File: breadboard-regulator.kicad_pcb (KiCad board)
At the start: 2 copper layers, 138.7 x 25.9 mm, 18 parts, among them J1 Barrel_Jack_Switch, J2 Conn_01x02_Pin, J3 Conn_01x02_Pin, U1 LM7805_TO220, U3 LD1117V33_TO-220

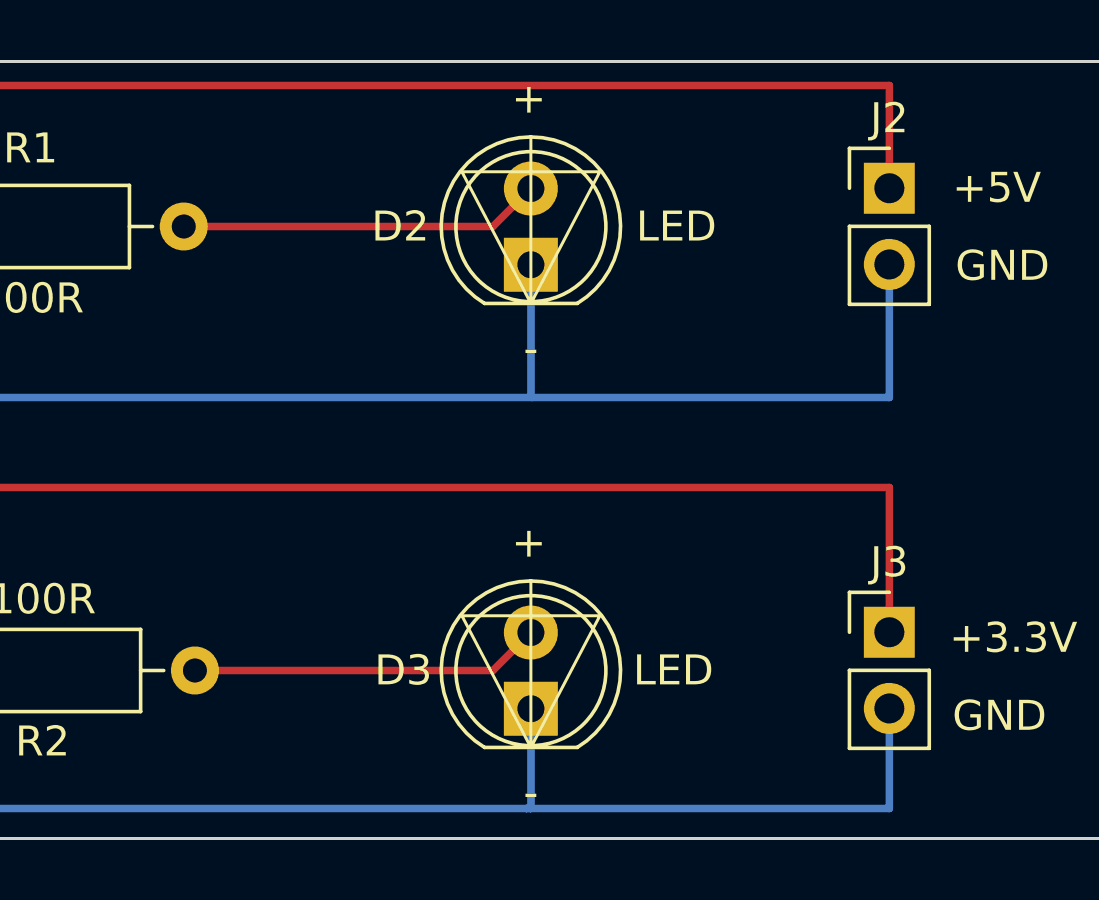
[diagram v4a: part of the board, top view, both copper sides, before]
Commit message: add new beginner pin header
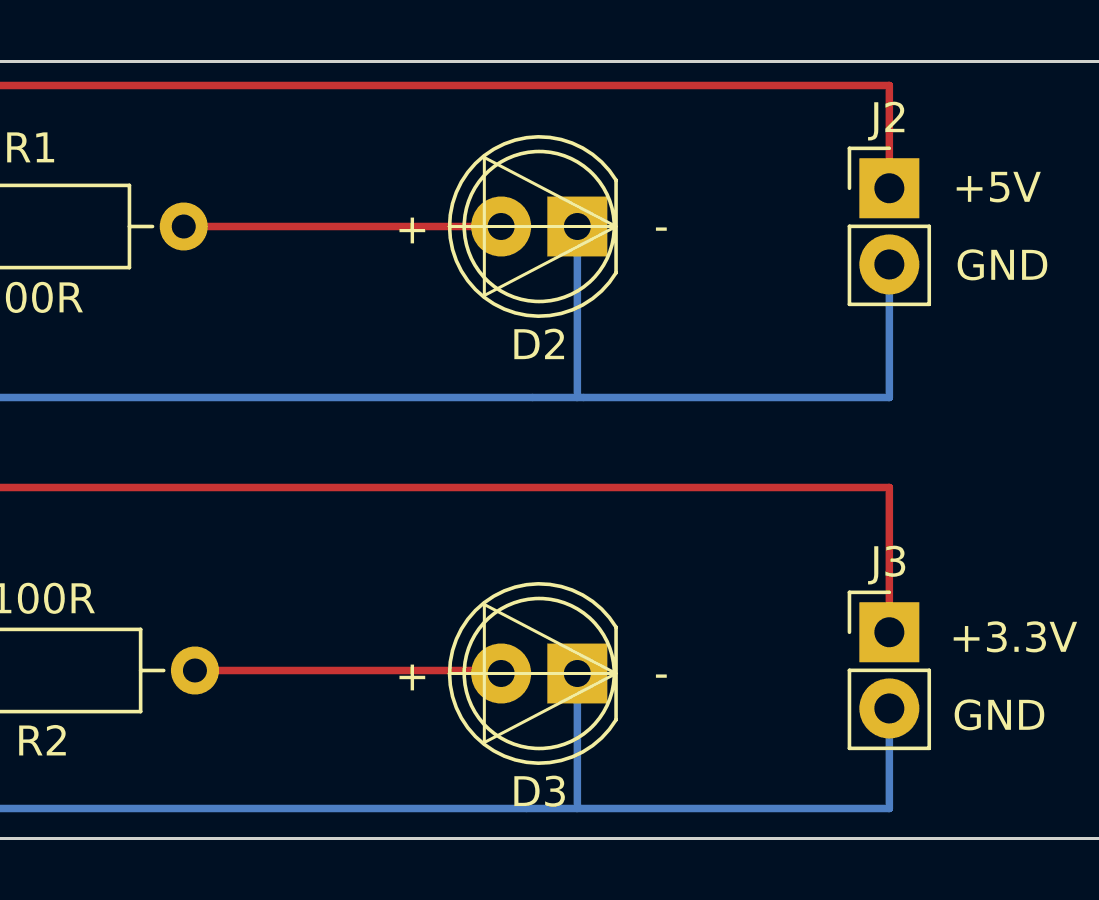
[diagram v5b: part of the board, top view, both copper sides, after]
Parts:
- D2, D3: footprint BeginnerModules:BeginnerLED_D5.0mm -> BeginnerModules:LED_D5.0mm
- J2, J3: footprint Connector_PinHeader_2.54mm:PinHeader_1x02_P2.54mm_Vertical -> BeginnerModules:PinHeader_1x02_P2.54mm_Vertical
- moved D2 2.01 mm to (197.7, 84.5), turned to 180 degrees
- moved D3 1.94 mm to (197.7, 99.4), turned to 180 degrees
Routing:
- net GNDREF: track 302.9 -> 305.2 mm
- net Net-(D2-A): track 12.1 -> 10.6 mm
- net Net-(D3-A): track 11.7 -> 10.2 mm
